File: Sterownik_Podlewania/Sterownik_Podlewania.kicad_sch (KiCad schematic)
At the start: 32 parts, among them J1 Screw_Terminal_01x02, J10 Conn_01x06_Socket, J11 Conn_01x06_Socket, J3 Conn_01x05_Pin, J4 Conn_01x05_Pin, J5 Conn_01x03_Pin, J7 Conn_01x05_Socket, J8 Conn_01x04_Pin, J9 Conn_01x06_Pin, SW7 SW_Nidec_CAS-120A1, U1 ESP32-DEVKITC, U2 L7805

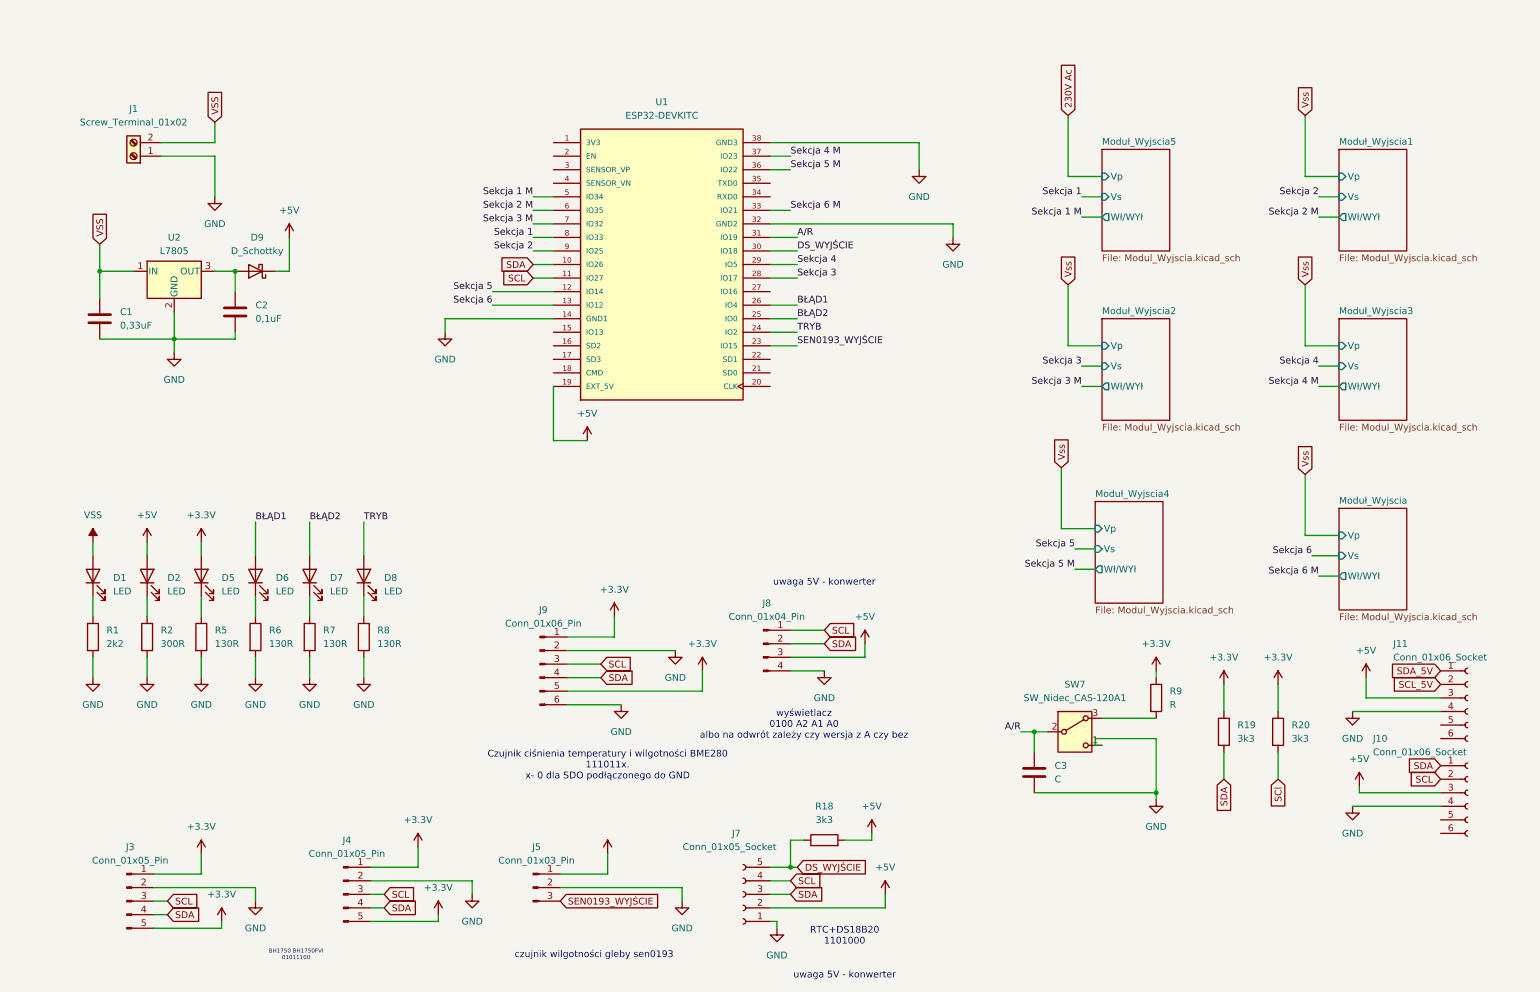
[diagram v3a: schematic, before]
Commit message: Dodanie większośi footprinów, dodanie osobno sekcji na 230V, dodanie jacka DC
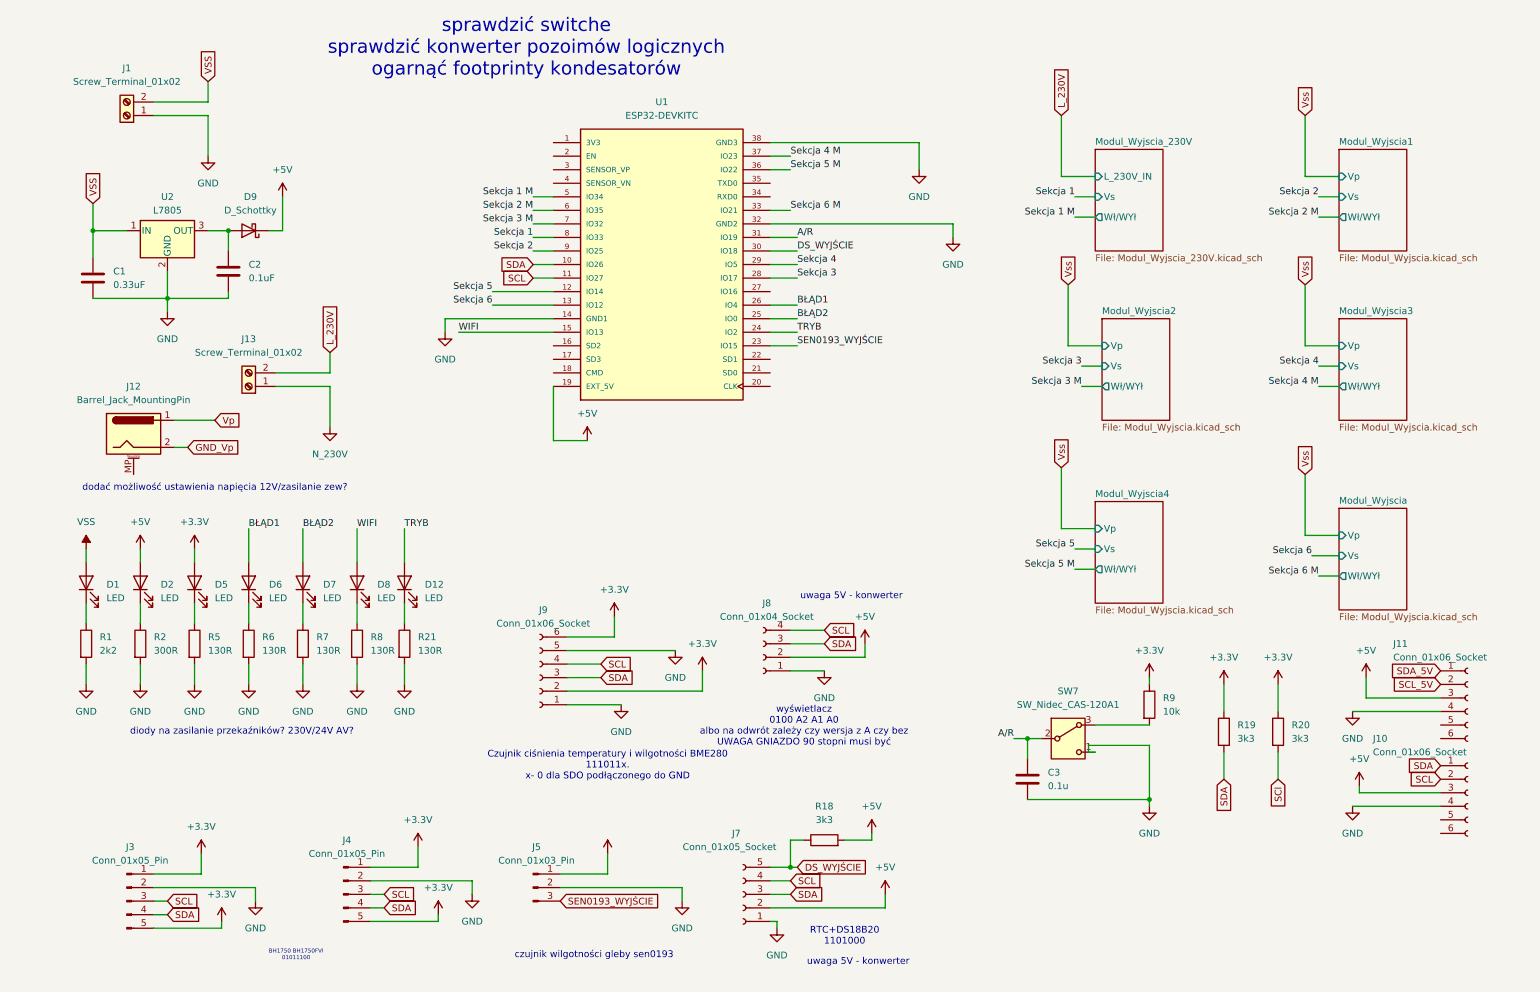
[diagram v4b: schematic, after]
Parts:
- removed J8: Conn_01x04_Pin, symbol Connector:Conn_01x04_Pin
- removed J9: Conn_01x06_Pin, symbol Connector:Conn_01x06_Pin
- added D12: LED, LED_SMD:LED_1206_3216Metric, symbol Device:LED
- added J12: Barrel_Jack_MountingPin, symbol Connector:Barrel_Jack_MountingPin
- added J13: Screw_Terminal_01x02, TerminalBlock:TerminalBlock_MaiXu_MX126-5.0-02P_1x02_P5.00mm, symbol Connector:Screw_Terminal_01x02
- added J8: Conn_01x04_Socket, Connector_Harwin:Harwin_M20-89006xx_1x06_P2.54mm_Horizontal, symbol Connector:Conn_01x04_Socket
- added J9: Conn_01x06_Socket, Connector_Harwin:Harwin_M20-89006xx_1x06_P2.54mm_Horizontal, symbol Connector:Conn_01x06_Socket
- added R21: 130R, Resistor_SMD:R_1206_3216Metric, symbol Device:R
- C1: value 0,33uF -> 0.33uF
- C2: value 0,1uF -> 0.1uF
- C3: value C -> 0.1u; footprint (none) -> Capacitor_SMD:C_1206_3216Metric
- D1, D2, D5, D6, D7, D8: footprint (none) -> LED_SMD:LED_1206_3216Metric
- J1: footprint (none) -> TerminalBlock:TerminalBlock_MaiXu_MX126-5.0-02P_1x02_P5.00mm
- J10, J11: footprint (none) -> Connector_Harwin:Harwin_M20-89006xx_1x06_P2.54mm_Horizontal
- J3, J4: footprint (none) -> Connector_Harwin:Harwin_M20-89005xx_1x05_P2.54mm_Horizontal
- J5: footprint (none) -> Connector_Harwin:Harwin_M20-89004xx_1x04_P2.54mm_Horizontal
- R1, R18, R19, R2, R20, R5, R6, R7, R8: footprint (none) -> Resistor_SMD:R_1206_3216Metric
- R9: value R -> 10k; footprint (none) -> Resistor_SMD:R_1206_3216Metric
- U2: footprint (none) -> Package_TO_SOT_THT:TO-220-3_Vertical
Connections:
- net +3.3V: now also J9.2 (Pin_2), J9.6 (Pin_6)
- net +5V: now also J8.2 (Pin_2)
- net GND: now also J8.1 (Pin_1), J9.1 (Pin_1), J9.5 (Pin_5), R21.2
- net SCL: now also J8.4 (Pin_4), J9.4 (Pin_4)
- net SDA: now also J8.3 (Pin_3), J9.3 (Pin_3)
- net TRYB: now also D12.2 (A); no longer D8.2 (A)
- net WIFI: now reaches U1.15 (IO13)
- net WIFI: now also D8.2 (A)
- new net: D12.1 (K), R21.1
- new net GND_Vp: J12.2
- new net L_230V: J13.2 (Pin_2)
- new net N_230V: J13.1 (Pin_1)
- new net Vp: J12.1
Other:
- sheet Moduł_Wyjscia renamed Modul_Wyjscia
- sheet Moduł_Wyjscia1 renamed Modul_Wyjscia1
- sheet Moduł_Wyjscia2 renamed Modul_Wyjscia2
- sheet Moduł_Wyjscia3 renamed Modul_Wyjscia3
- sheet Moduł_Wyjscia4 renamed Modul_Wyjscia4
- removed sheet Moduł_Wyjscia5
- added sheet Modul_Wyjscia_230V (Modul_Wyjscia_230V.kicad_sch)
- note added: "diody na zasilanie przekaźników? 230V/24V AV?"
- note added: "dodać możliwość ustawienia napięcia 12V/zasilanie zew?"
- note added: "sprawdzić switche sprawdzić konwerter pozoimów logicznych ogarnąć footprinty kondesatorów"
- note added: "wyświetlacz 0100 A2 A1 A0 albo na odwrót zależy czy wersja z A czy bez UWAGA GNIAZDO 90 stopni musi być"
- note removed: "wyświetlacz 0100 A2 A1 A0 albo na odwrót zależy czy wersja z A czy bez"
- moved on the sheet: C1, C2, C3, D1, D2, D5, D6, D7, D8, D9, J1, R1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

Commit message: Dodanie dokumentacji przełączników, sprawdzenie konwertera I2C, dodanie sekcji przełącznika, dodanie DIP swticha do przełączania zasialania zew, wydzielenie sekcji zasilania
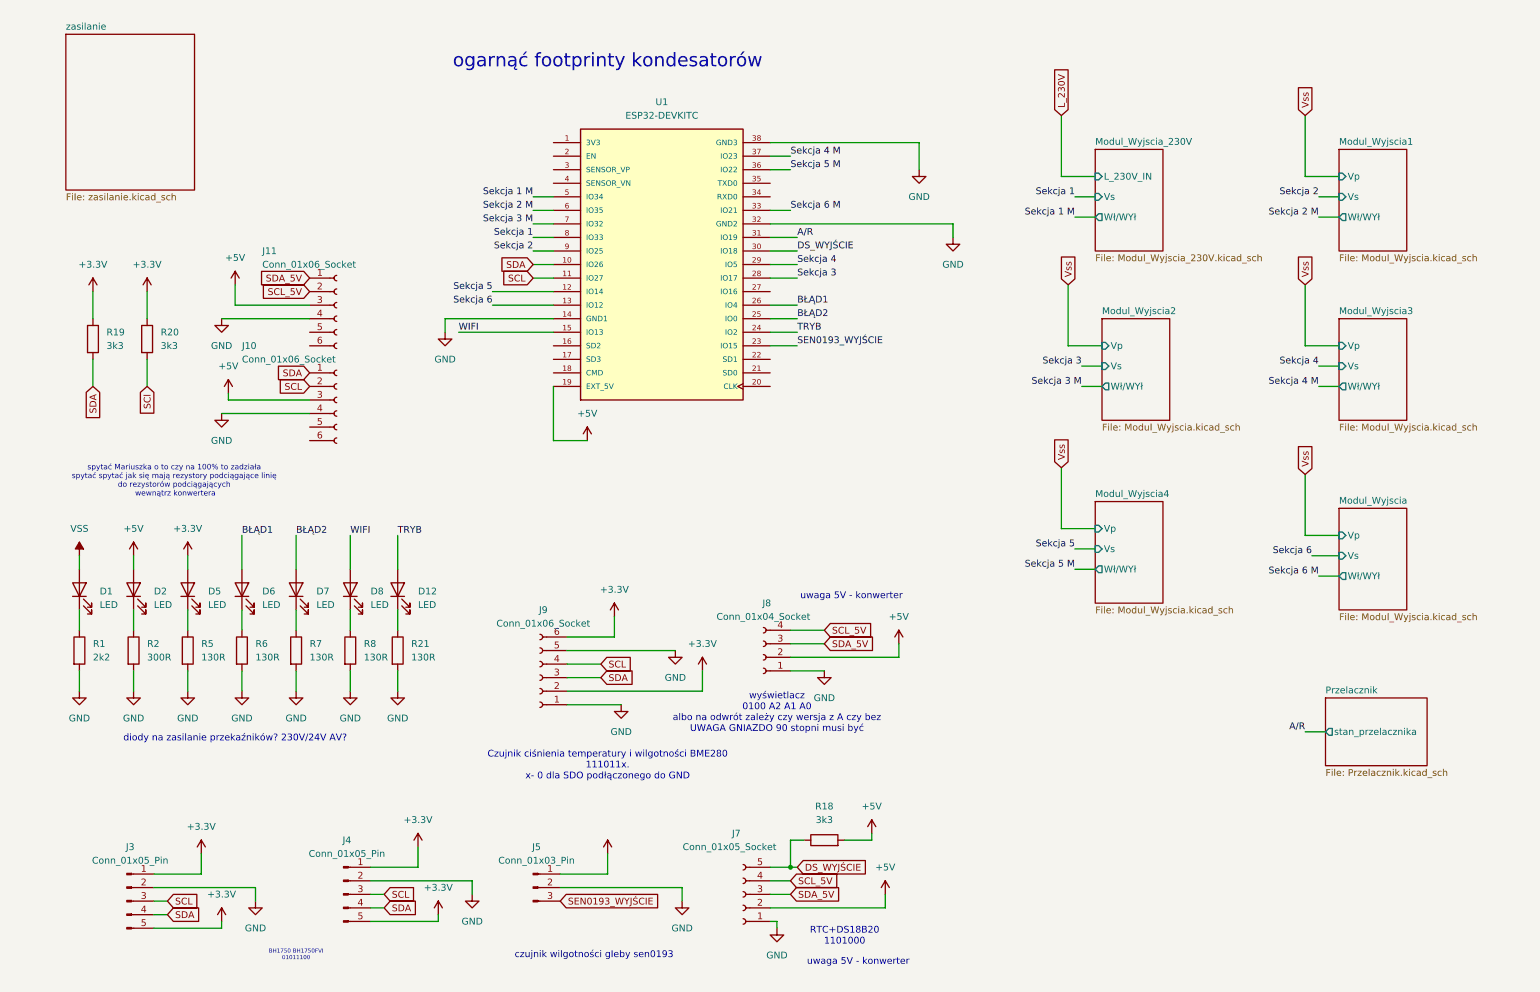
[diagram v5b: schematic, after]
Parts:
- removed C1: 0.33uF, symbol Device:C
- removed C2: 0.1uF, symbol Device:C
- removed C3: 0.1u, Capacitor_SMD:C_1206_3216Metric, symbol Device:C
- removed D9: D_Schottky, symbol Device:D_Schottky
- removed J1, J13: Screw_Terminal_01x02, TerminalBlock:TerminalBlock_MaiXu_MX126-5.0-02P_1x02_P5.00mm, symbol Connector:Screw_Terminal_01x02
- removed J12: Barrel_Jack_MountingPin, symbol Connector:Barrel_Jack_MountingPin
- removed R9: 10k, Resistor_SMD:R_1206_3216Metric, symbol Device:R
- removed SW7: SW_Nidec_CAS-120A1, Button_Switch_SMD:Nidec_Copal_CAS-120A, symbol Switch:SW_Nidec_CAS-120A1
- removed U2: L7805, Package_TO_SOT_THT:TO-220-3_Vertical, symbol Regulator_Linear:L7805
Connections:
- net SCL: no longer J7.4 (Pin_4), J8.4 (Pin_4)
- net SCL_5V: now also J7.4 (Pin_4), J8.4 (Pin_4)
- net SDA: no longer J7.3 (Pin_3), J8.3 (Pin_3)
- net SDA_5V: now also J7.3 (Pin_3), J8.3 (Pin_3)
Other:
- added sheet Przelacznik (Przelacznik.kicad_sch)
- added sheet zasilanie (zasilanie.kicad_sch)
- note added: "ogarnąć footprinty kondesatorów"
- note added: "spytać Mariuszka o to czy na 100% to zadziała spytać spytać jak się mają rezystory podciągające linię do rezystorów podciągających wewnątrz konwertera"
- note removed: "dodać możliwość ustawienia napięcia 12V/zasilanie zew?"
- note removed: "sprawdzić switche sprawdzić konwerter pozoimów logicznych ogarnąć footprinty kondesatorów"
- moved on the sheet: D1, D12, D2, D5, D6, D7, D8, J10, J11, R1, R19, R2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

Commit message: Poprawki estetyczne schematu
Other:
- title: (none) -> Sterownik podlewania
- moved on the sheet: D1, D12, D2, D5, D6, D7, D8, J10, J11, J7, J8, J9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
